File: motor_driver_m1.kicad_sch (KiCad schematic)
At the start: 45 parts, among them J2 Conn_01x01_Pin, J4 Conn_01x01_Pin, J5 Conn_01x01_Pin, J6 Conn_01x01_Pin, Q1 NP80N06D6, Q2 NP80N06D6, Q3 NP80N06D6, Q4 NP80N06D6, Q5 NP80N06D6, Q6 NP80N06D6, U2 STM32C011F6U6TR, U3 STDRIVE101

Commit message: ...
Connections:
- net DShot_M1: now also U2.6 (PA1)
- net PHASE_A_M1: now also U2.7 (PA2); no longer U2.8 (PA3)
- net PHASE_B_M1: now also U2.8 (PA3); no longer U2.7 (PA2)
- net SWCLK renamed SWCLK_H
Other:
- title: (none) -> MOTOR DRIVER M1
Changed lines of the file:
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@@
 	(generator_version "10.0")
 	(paper "A4")
+	(title_block
+		(title "MOTOR DRIVER M1")
+		(rev "1.0")
+	)
 	(text_box "DShot\n"
 		(exclude_from_sim no)
@@
 		)
 	)
+	(global_label "DShot_M1"
+		(shape input)
+		(at 64.77 57.15 180)
+		(fields_autoplaced yes)
+		(effects
+			(font
+				(size 1.27 1.27)
+			)
+			(justify right)
+		)
+		(property "Intersheetrefs" "${INTERSHEET_REFS}"
+			(at 52.6531 57.15 0)
+			(hide yes)
+			(show_name no)
+			(do_not_autoplace no)
+			(effects
+				(font
+					(size 1.27 1.27)
+				)
+				(justify right)
+			)
+		)
+	)
 	(global_label "INH1_M1"
 		(shape input)
@@
 		)
 	)
-	(global_label "PHASE_A_M1"
+	(global_label "PHASE_B_M1"
 		(shape input)
 		(at 64.77 62.23 180)
@@
 		)
 		(property "Intersheetrefs" "${INTERSHEET_REFS}"
-			(at 50.0525 62.23 0)
+			(at 49.8711 62.23 0)
 			(hide yes)
 			(show_name no)
@@
 		)
 	)
-	(global_label "PHASE_B_M1"
+	(global_label "PHASE_A_M1"
 		(shape input)
 		(at 64.77 59.69 180)
@@
 		)
 		(property "Intersheetrefs" "${INTERSHEET_REFS}"
-			(at 49.8711 59.69 0)
+			(at 50.0525 59.69 0)
 			(hide yes)
 			(show_name no)
@@
 		)
 	)
-	(global_label "SWCLK"
+	(global_label "SWCLK_H"
 		(shape input)
 		(at 118.11 52.07 0)
@@
 		)
 		(property "Intersheetrefs" "${INTERSHEET_REFS}"
-			(at 127.3242 52.07 0)
+			(at 129.6223 52.07 0)
 			(hide yes)
 			(show_name no)

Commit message: ...
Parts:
- J2: footprint deshan:Conn_1x1_small -> deshan:Conn_01x01_Pin
- J4, J5, J6: footprint deshan:Conn_1x1 -> deshan:Conn_01x01_Power
- renumbered C56 to C1, C51 to C10, C58 to C11, C59 to C12, C24 to C13, C25 to C14, C26 to C15, C12 to C2, C55 to C3, C20 to C4, C6 to C5, C7 to C6, C8 to C7, C9 to C8, C10 to C9, R6 to R1, R12 to R10, R13 to R11, R14 to R12, R15 to R13, R16 to R14, R17 to R15, R18 to R16, R19 to R17, R20 to R18, R4 to R2, R7 to R3, R35 to R4, R3 to R5, R8 to R6, R9 to R7, R10 to R8, R11 to R9
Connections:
- net PHASE_A_M1: now also U2.9 (PA4); no longer U2.7 (PA2)
- net PHASE_C_M1: now also U2.7 (PA2); no longer U2.9 (PA4)
- net SWCLK_H renamed SWCLK_M1

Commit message: ...
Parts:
- renumbered J2 to DShot_M1, U3 to GD1, J4 to J1, J5 to J2, J6 to J3, U2 to M1
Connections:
- no-connect marks 2 -> 5
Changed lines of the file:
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@@
 	)
 	(junction
-		(at 55.88 49.53)
+		(at 55.88 24.13)
 		(diameter 0)
 		(color 0 0 0 0)
 	)
 	(junction
-		(at 109.22 175.26)
+		(at 55.88 49.53)
 		(diameter 0)
 		(color 0 0 0 0)
 	)
 	(junction
-		(at 119.38 107.95)
+		(at 109.22 175.26)
 		(diameter 0)
 		(color 0 0 0 0)
 	)
 	(junction
-		(at 55.88 24.13)
+		(at 119.38 107.95)
 		(diameter 0)
 		(color 0 0 0 0)
@@
 	)
 	(no_connect
+		(at 118.11 49.53)
+	)
+	(no_connect
 		(at 64.77 44.45)
 	)
@@
 		(at 118.11 44.45)
 	)
+	(no_connect
+		(at 118.11 46.99)
+	)
+	(no_connect
+		(at 64.77 54.61)
+	)
 	(wire
 		(pts
@@
 	(wire
 		(pts
-			(xy 64.77 46.99) (xy 59.69 46.99)
+			(xy 59.69 46.99) (xy 64.77 46.99)
 		)
 		(stroke
@@
 		(dnp no)
 		(fields_autoplaced yes)
-		(property "Reference" "U2"
+		(property "Reference" "M1"
 			(at 91.44 36.83 0)
 			(show_name no)
@@
 			(project "esc"
 				(path "/131092d7-5dad-4272-a758-a2445b6ec99c/63f0bd9c-70c2-4847-814d-8da099671243"
-					(reference "U2")
+					(reference "M1")
 					(unit 1)
 				)
@@
 		(dnp no)
 		(fields_autoplaced yes)
-		(property "Reference" "U3"
+		(property "Reference" "GD1"
 			(at 81.28 95.25 0)
 			(show_name no)
@@
 			(project "esc"
 				(path "/131092d7-5dad-4272-a758-a2445b6ec99c/63f0bd9c-70c2-4847-814d-8da099671243"
-					(reference "U3")
+					(reference "GD1")
 					(unit 1)
 				)
@@
 		(dnp no)
 		(fields_autoplaced yes)
-		(property "Reference" "J4"
+		(property "Reference" "J1"
 			(at 154.305 160.02 0)
 			(show_name no)
@@
 			(project "esc"
 				(path "/131092d7-5dad-4272-a758-a2445b6ec99c/63f0bd9c-70c2-4847-814d-8da099671243"
-					(reference "J4")
+					(reference "J1")
 					(unit 1)
 				)
@@
 		(in_pos_files yes)
 		(dnp no)
-		(property "Reference" "J5"
+		(property "Reference" "J2"
 			(at 154.305 168.91 0)
 			(show_name no)
@@
 			(project "esc"
 				(path "/131092d7-5dad-4272-a758-a2445b6ec99c/63f0bd9c-70c2-4847-814d-8da099671243"
-					(reference "J5")
+					(reference "J2")
 					(unit 1)
 				)
@@
 		(dnp no)
 		(fields_autoplaced yes)
-		(property "Reference" "J6"
+		(property "Reference" "J3"
 			(at 154.305 179.07 0)
 			(show_name no)
@@
 			(project "esc"
 				(path "/131092d7-5dad-4272-a758-a2445b6ec99c/63f0bd9c-70c2-4847-814d-8da099671243"
-					(reference "J6")
+					(reference "J3")
 					(unit 1)
 				)
@@
 		(dnp no)
 		(fields_autoplaced yes)
-		(property "Reference" "J2"
+		(property "Reference" "DShot_M1"
 			(at 165.1 127.6349 90)
 			(show_name no)
@@
 			(project "esc"
 				(path "/131092d7-5dad-4272-a758-a2445b6ec99c/63f0bd9c-70c2-4847-814d-8da099671243"
-					(reference "J2")
+					(reference "DShot_M1")
 					(unit 1)
 				)

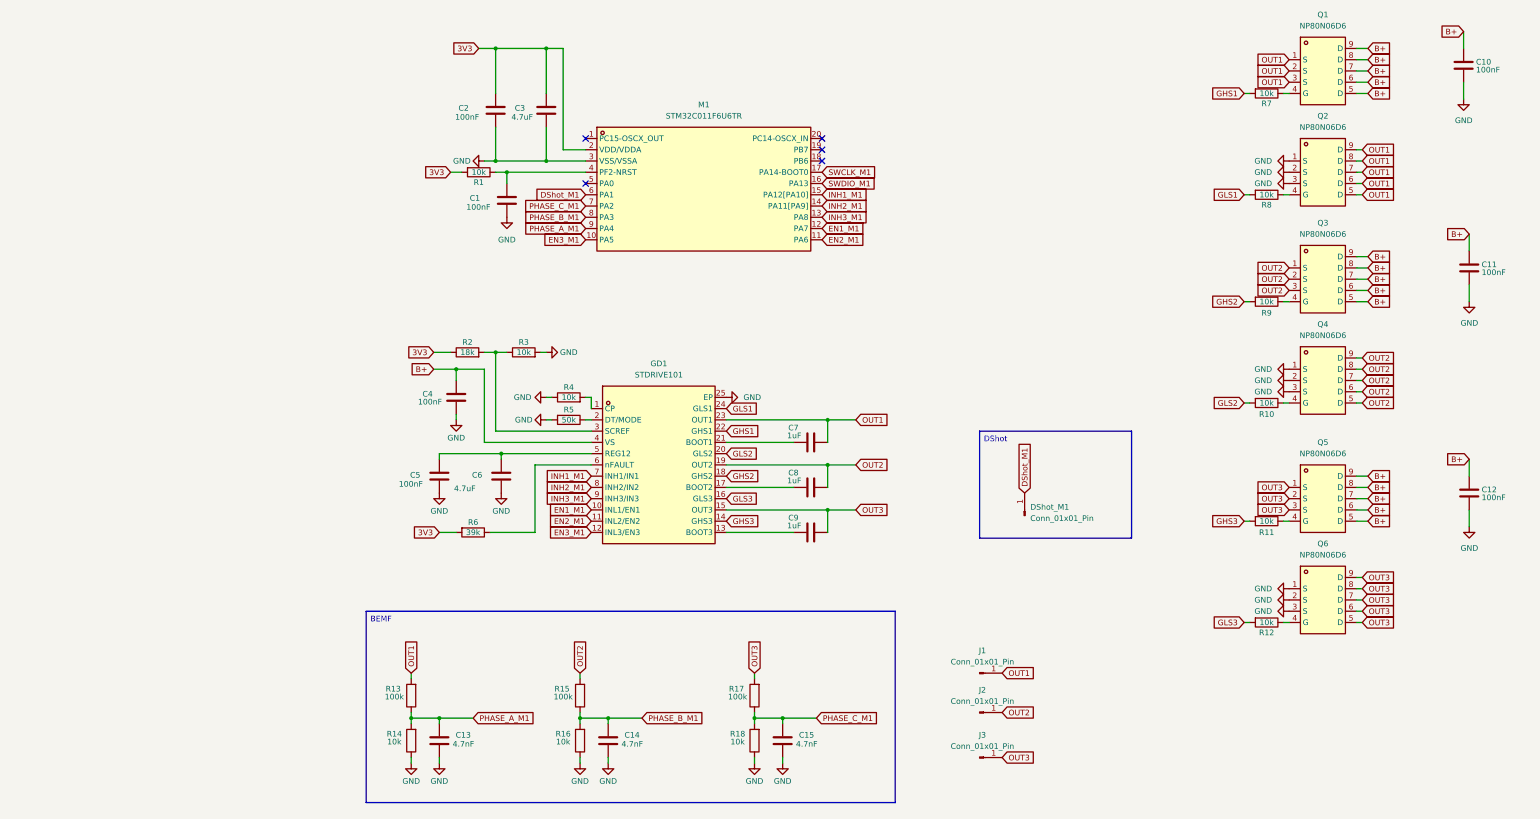
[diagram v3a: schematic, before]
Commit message: change in architecture with horizonatal half bridge
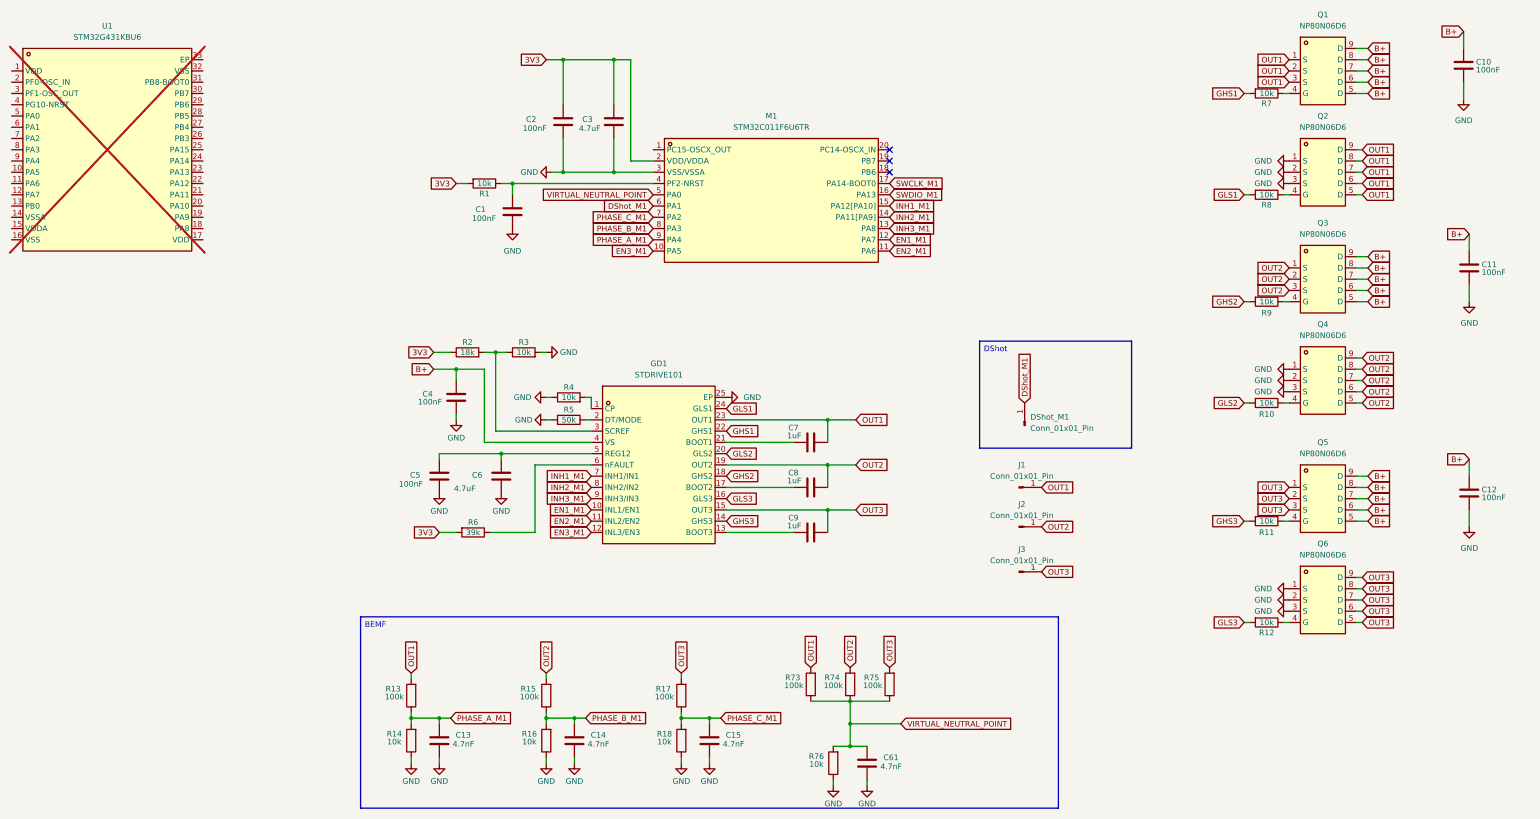
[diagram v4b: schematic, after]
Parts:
- added C61: 4.7nF, easyeda2kicad:C0402, symbol Device:C
- added R73, R74, R75: 100k, easyeda2kicad:R0402, symbol Device:R
- added R76: 10k, easyeda2kicad:R0402, symbol Device:R
- added U1: STM32G431KBU6, easyeda2kicad:QFN-32_L5.0-W5.0-P0.50-BL-EP3.7, symbol easyeda2kicad:STM32G431KBU6
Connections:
- net GND: now also C61.2, R76.1
- net OUT1: now also R73.2
- net OUT2: now also R74.2
- net OUT3: now also R75.2
- net VIRTUAL_NEUTRAL_POINT: now reaches M1.5 (PA0)
- net VIRTUAL_NEUTRAL_POINT: now also C61.1, R73.1, R74.1, R75.1, R76.2
- no-connect marks 5 -> 3
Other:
- moved on the sheet: C1, C14, C15, C2, C3, DShot_M1, J1, J2, J3, R1, R15, R16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

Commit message: ...
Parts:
- removed U1: STM32G431KBU6, easyeda2kicad:QFN-32_L5.0-W5.0-P0.50-BL-EP3.7, symbol easyeda2kicad:STM32G431KBU6
- added SWCLK_M1, SWDIO_M1: Conn_01x01_Pin, deshan:Conn_01x01_Pin, symbol Connector:Conn_01x01_Pin
- R2: value 18k -> 100k
- R3: value 10k -> 18k
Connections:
- net SWCLK_M1: now also SWCLK_M1.1 (Pin_1)
- net SWDIO_M1: now also SWDIO_M1.1 (Pin_1)
- no-connect marks 3 -> 4
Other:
- moved on the sheet: C10, C11, C12, C13, C14, C15, C2, C3, C4, C5, C6, C61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
